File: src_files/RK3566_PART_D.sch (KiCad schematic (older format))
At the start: 52 parts, among them Q6 DTC143ZEBTL, Q7 DTC143ZEBTL, U1 RK3566, U4 LPDDR4_32_IS43LQ32128A-062BLI, Y3 24MHz/10ppm

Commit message: wireless power TX RX added
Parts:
- R71: footprint Resistor_SMD:R_0402_1005Metric_Pad0.72x0.64mm_HandSolder -> Resistor_SMD:R_0402_1005Metric
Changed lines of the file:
@@
 $Descr A3 16535 11693
 encoding utf-8
-Sheet 6 15
+Sheet 6 16
 Title ""
 Date ""
@@
 F 0 "R71" V 1655 10525 50  0000 C CNN
 F 1 "100R" V 1564 10525 50  0000 C CNN
-F 2 "Resistor_SMD:R_0402_1005Metric_Pad0.72x0.64mm_HandSolder" V 1490 10515 50  0001 C CNN
+F 2 "Resistor_SMD:R_0402_1005Metric" V 1490 10515 50  0001 C CNN
 F 3 "~" H 1450 10525 50  0001 C CNN
 	1    1450 10525

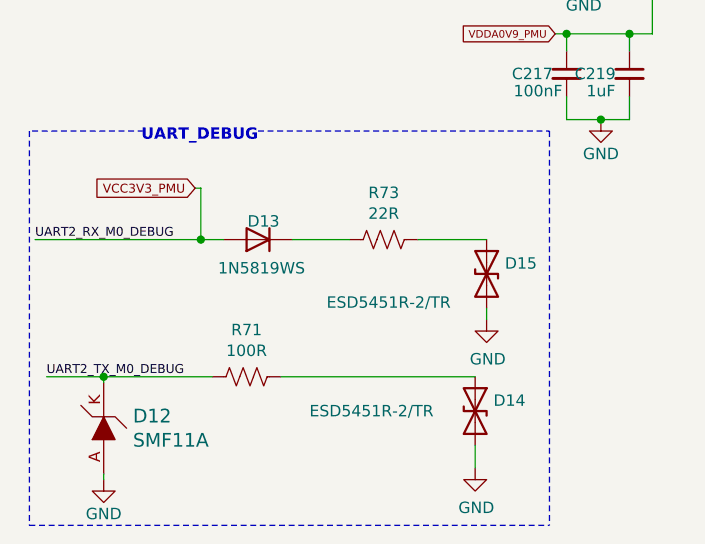
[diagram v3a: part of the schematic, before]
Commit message: updates rules check and associations
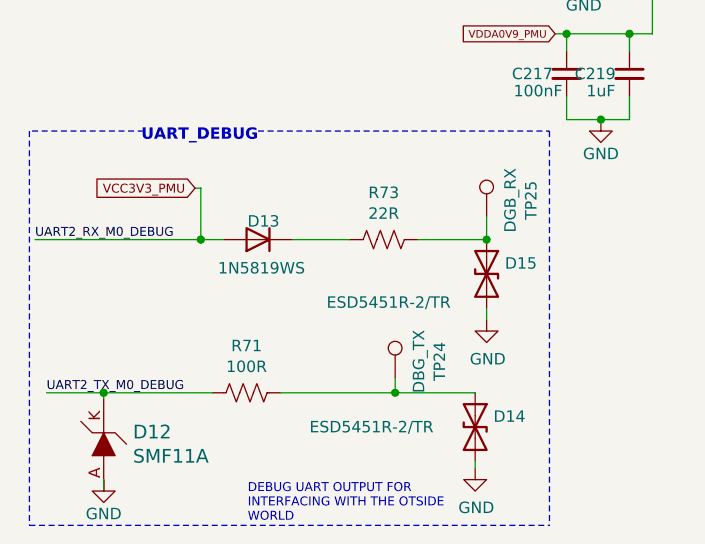
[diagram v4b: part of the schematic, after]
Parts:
- added TP24: DBG_TX, TestPoint:TestPoint_Pad_1.0x1.0mm, symbol Connector:TestPoint
- added TP25: DGB_RX, TestPoint:TestPoint_Pad_1.0x1.0mm, symbol Connector:TestPoint
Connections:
- net at D15.1 (A1), R73.2: now also TP25.1
- net at D14.1 (A1), R71.2: now also TP24.1
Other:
- note added: "DEBUG UART OUTPUT FOR\nINTERFACING WITH THE OTSIDE\nWORLD"
- moved on the sheet: D12, D14, R71
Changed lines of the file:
@@
 Text Label 7600 9350 0    39   ~ 0
 UART2_TX_M0_DEBUG
-Text Label 575  10525 0    39   ~ 0
+Text Label 575  10595 0    39   ~ 0
 UART2_TX_M0_DEBUG
 Connection ~ 1375 6325
@@
 L Device:D_TVS D?
 U 1 1 6563491E
-P 2450 10675
+P 2450 10745
 AR Path="/61C73AB6/6563491E" Ref="D?"  Part="1"
 AR Path="/61E38FEF/6563491E" Ref="D14"  Part="1"
-F 0 "D14" V 2404 10755 50  0000 L CNN
-F 1 "ESD5451R-2/TR" V 2450 9950 50  0000 L CNN
-F 2 "greencharge-footprints:DFP1006-2L" H 2450 10675 50  0001 C CNN
-F 3 "~" H 2450 10675 50  0001 C CNN
-	1    2450 10675
+F 0 "D14" V 2404 10825 50  0000 L CNN
+F 1 "ESD5451R-2/TR" V 2450 10020 50  0000 L CNN
+F 2 "greencharge-footprints:DFP1006-2L" H 2450 10745 50  0001 C CNN
+F 3 "~" H 2450 10745 50  0001 C CNN
+	1    2450 10745
 	0    1    1    0
 $EndComp
@@
 L dk_TVS-Diodes:ESD5Z3_3T1G D?
 U 1 1 6566C1E5
-P 825 10750
+P 825 10820
 AR Path="/64C7F7B0/6566C1E5" Ref="D?"  Part="1"
 AR Path="/61E38FEF/6566C1E5" Ref="D12"  Part="1"
-F 0 "D12" V 878 10622 60  0000 R CNN
-F 1 "SMF11A" V 772 10622 60  0000 R CNN
-F 2 "Diode_SMD:D_SOD-123" H 1025 10950 60  0001 L CNN
-F 3 "https://www.onsemi.com/pub/Collateral/ESD5Z2.5T1-D.PDF" H 1025 11050 60  0001 L CNN
-F 4 "SMF11A" H 1025 11150 60  0001 L CNN "Digi-Key_PN"
-F 5 "SMF11A" H 1025 11250 60  0001 L CNN "MPN"
-	1    825  10750
+F 0 "D12" V 878 10692 60  0000 R CNN
+F 1 "SMF11A" V 772 10692 60  0000 R CNN
+F 2 "Diode_SMD:D_SOD-123" H 1025 11020 60  0001 L CNN
+F 3 "https://www.onsemi.com/pub/Collateral/ESD5Z2.5T1-D.PDF" H 1025 11120 60  0001 L CNN
+F 4 "SMF11A" H 1025 11220 60  0001 L CNN "Digi-Key_PN"
+F 5 "SMF11A" H 1025 11320 60  0001 L CNN "MPN"
+	1    825  10820
 	0    -1   -1   0
 $EndComp
@@
 L Device:R_US R71
 U 1 1 6568E3B7
-P 1450 10525
-F 0 "R71" V 1655 10525 50  0000 C CNN
-F 1 "100R" V 1564 10525 50  0000 C CNN
-F 2 "Resistor_SMD:R_0402_1005Metric" V 1490 10515 50  0001 C CNN
-F 3 "~" H 1450 10525 50  0001 C CNN
-	1    1450 10525
+P 1450 10595
+F 0 "R71" V 1655 10595 50  0000 C CNN
+F 1 "100R" V 1564 10595 50  0000 C CNN
+F 2 "Resistor_SMD:R_0402_1005Metric" V 1490 10585 50  0001 C CNN
+F 3 "~" H 1450 10595 50  0001 C CNN
+	1    1450 10595
 	0    -1   -1   0
 $EndComp
 Wire Wire Line
-	575  10525 825  10525
-Wire Wire Line
-	825  10550 825  10525
-Connection ~ 825  10525
+	575  10595 825  10595
+Wire Wire Line
+	825  10620 825  10595
+Connection ~ 825  10595
 $Comp
 L OLIMEX_Power:GND #PWR0208
@@
 $EndComp
 Wire Wire Line
-	825  10975 825  10950
-Wire Wire Line
-	825  10525 1300 10525
-Wire Wire Line
-	2450 10925 2450 10825
-Wire Wire Line
-	1600 10525 2450 10525
+	825  10975 825  11020
+Wire Wire Line
+	825  10595 1300 10595
+Wire Wire Line
+	2450 10925 2450 10895
+Wire Wire Line
+	1600 10595 2100 10595
 Text Notes 1500 9500 2    50   ~ 10
 UART_DEBUG
@@
 	3150 7950 3350 7950
 NoConn ~ 12250 6250
+$Comp
+L Connector:TestPoint TP?
+U 1 1 63AB0166
+P 2100 10530
+AR Path="/6823D52E/63AB0166" Ref="TP?"  Part="1"
+AR Path="/61E38FEF/63AB0166" Ref="TP24"  Part="1"
+F 0 "TP24" V 2295 10602 50  0000 C CNN
+F 1 "DBG_TX" V 2204 10602 50  0000 C CNN
+F 2 "TestPoint:TestPoint_Pad_1.0x1.0mm" H 2300 10530 50  0001 C CNN
+F 3 "~" H 2300 10530 50  0001 C CNN
+	1    2100 10530
+	1    0    0    -1
+$EndComp
+$Comp
+L Connector:TestPoint TP?
+U 1 1 63AB016C
+P 2500 9825
+AR Path="/6823D52E/63AB016C" Ref="TP?"  Part="1"
+AR Path="/61E38FEF/63AB016C" Ref="TP25"  Part="1"
+F 0 "TP25" V 2695 9897 50  0000 C CNN
+F 1 "DGB_RX" V 2604 9897 50  0000 C CNN
+F 2 "TestPoint:TestPoint_Pad_1.0x1.0mm" H 2700 9825 50  0001 C CNN
+F 3 "~" H 2700 9825 50  0001 C CNN
+	1    2500 9825
+	1    0    0    -1
+$EndComp
+Wire Wire Line
+	2500 9925 2500 9825
+Connection ~ 2500 9925
+Wire Wire Line
+	2100 10530 2100 10595
+Connection ~ 2100 10595
+Wire Wire Line
+	2100 10595 2450 10595
+Text Notes 1455 11165 0    39   ~ 0
+DEBUG UART OUTPUT FOR\nINTERFACING WITH THE OTSIDE\nWORLD
 $EndSCHEMATC
